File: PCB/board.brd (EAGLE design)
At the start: 100 x 80 mm, 11 parts, among them Q1 16 MHz, U1 ATMEGA16U2AU

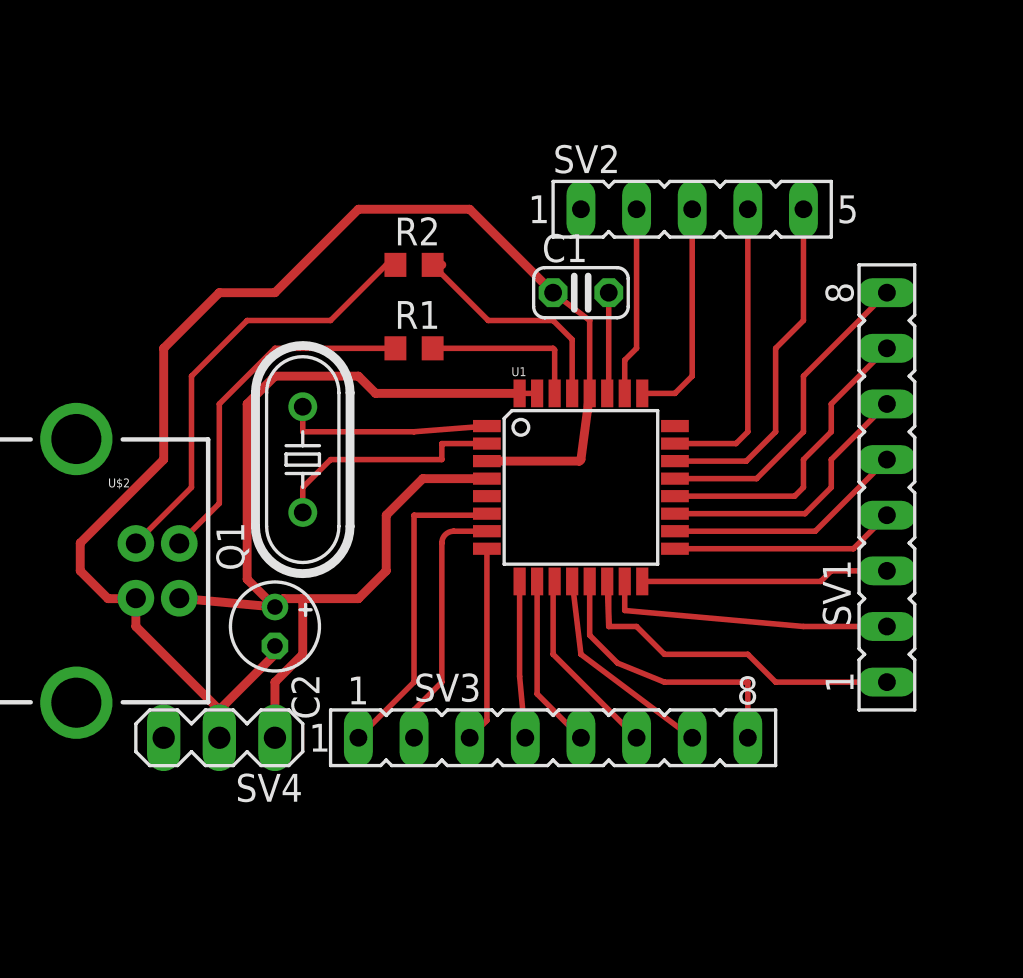
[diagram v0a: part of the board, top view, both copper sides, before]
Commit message: fixed PCB design
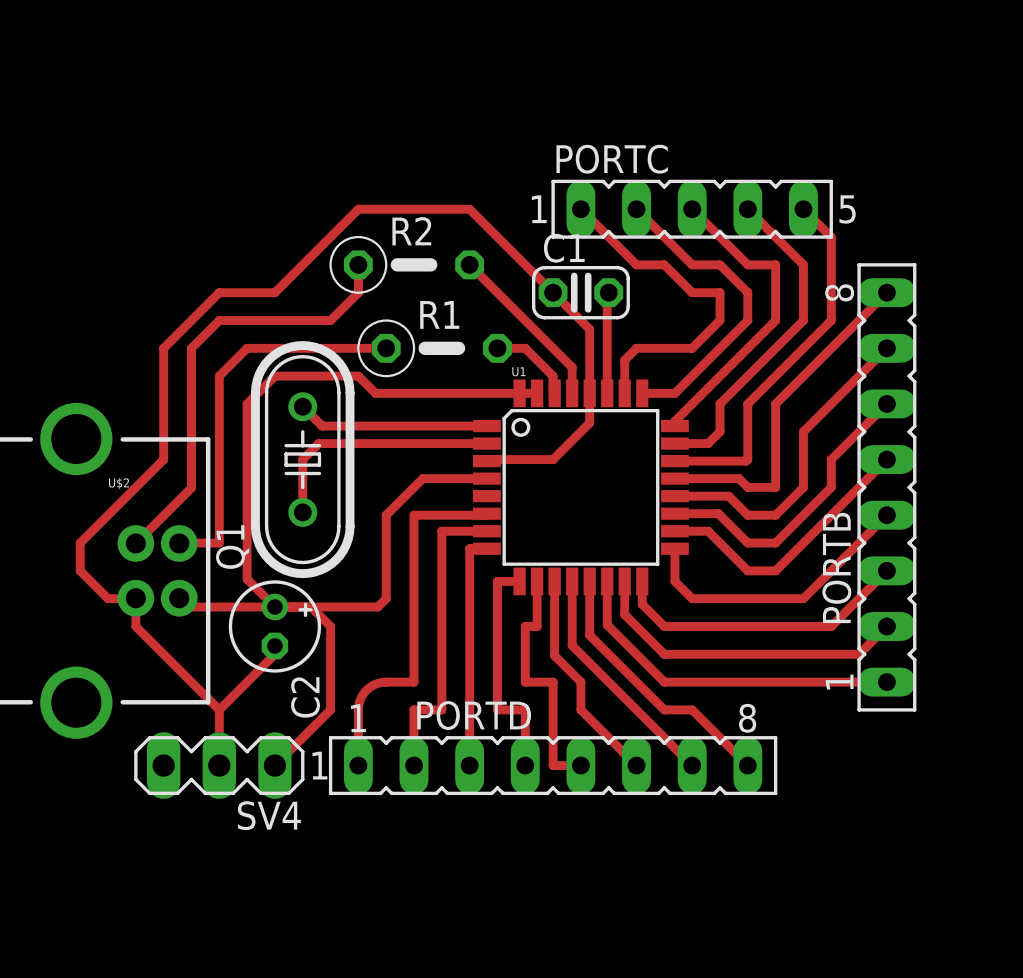
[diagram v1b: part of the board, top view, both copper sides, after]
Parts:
- removed SV3: (no value), con-lsta:FE08
- added PORTD: (no value), con-lsta:FE08
- R1, R2: device resistor:R0603 -> rcl:0207/5V
- moved R1 1.27 mm to (49.5, 45.7)
- moved SV4 1.27 mm to (39.4, 26.7)
- renumbered SV1 to PORTB, SV2 to PORTC
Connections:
- new net N$33: PORTC.3, U1.24
- net N$18: now also PORTD.8; no longer SV3.8
- net N$19: now also U1.25; no longer U1.26
- net N$2: now also PORTD.6; no longer SV3.6
- net N$20: now also PORTC.1, U1.26; no longer PORTC.3, U1.25
- net N$23: now also PORTD.7; no longer SV3.7
- net N$25: now also PORTD.5; no longer SV3.5
- net N$26: now also PORTD.4; no longer SV3.4
- net N$27: now also PORTD.3; no longer SV3.3
- net N$28: now also PORTD.2; no longer SV3.2
- net N$29: now also PORTD.1; no longer SV3.1
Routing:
- net N$33: track 0.00 -> 14.1 mm
- net N$20: track 10.2 -> 15.8 mm
- net N$19: track 8.63 -> 14.1 mm
- net N$6: track 48.7 -> 53.1 mm
- net N$4: track 7.59 -> 3.88 mm
- net N$26: track 7.15 -> 10.7 mm
- net N$25: track 7.97 -> 11.5 mm
- net N$11: track 10.7 -> 7.81 mm
- net N$7: track 10.3 -> 13.1 mm
- net N$12: track 18.4 -> 15.8 mm
- net N$28: track 11.7 -> 14.0 mm
- net N$31: track 11.4 -> 13.7 mm
- net N$29: track 14.6 -> 16.6 mm
- net N$27: track 8.96 -> 10.7 mm
- net N$14: track 11.0 -> 12.5 mm
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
